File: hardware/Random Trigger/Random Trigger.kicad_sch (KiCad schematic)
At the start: 69 parts, among them J1 Eurorack Power, J10 Trigger Out B, J11 Inv Trigger Out B, J2 Noise In, J3 Noise Out, J4 Trigger In A, J5 Gate Out A, J6 Trigger Out A, J7 Inv Trigger Out A, J8 Trigger In B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

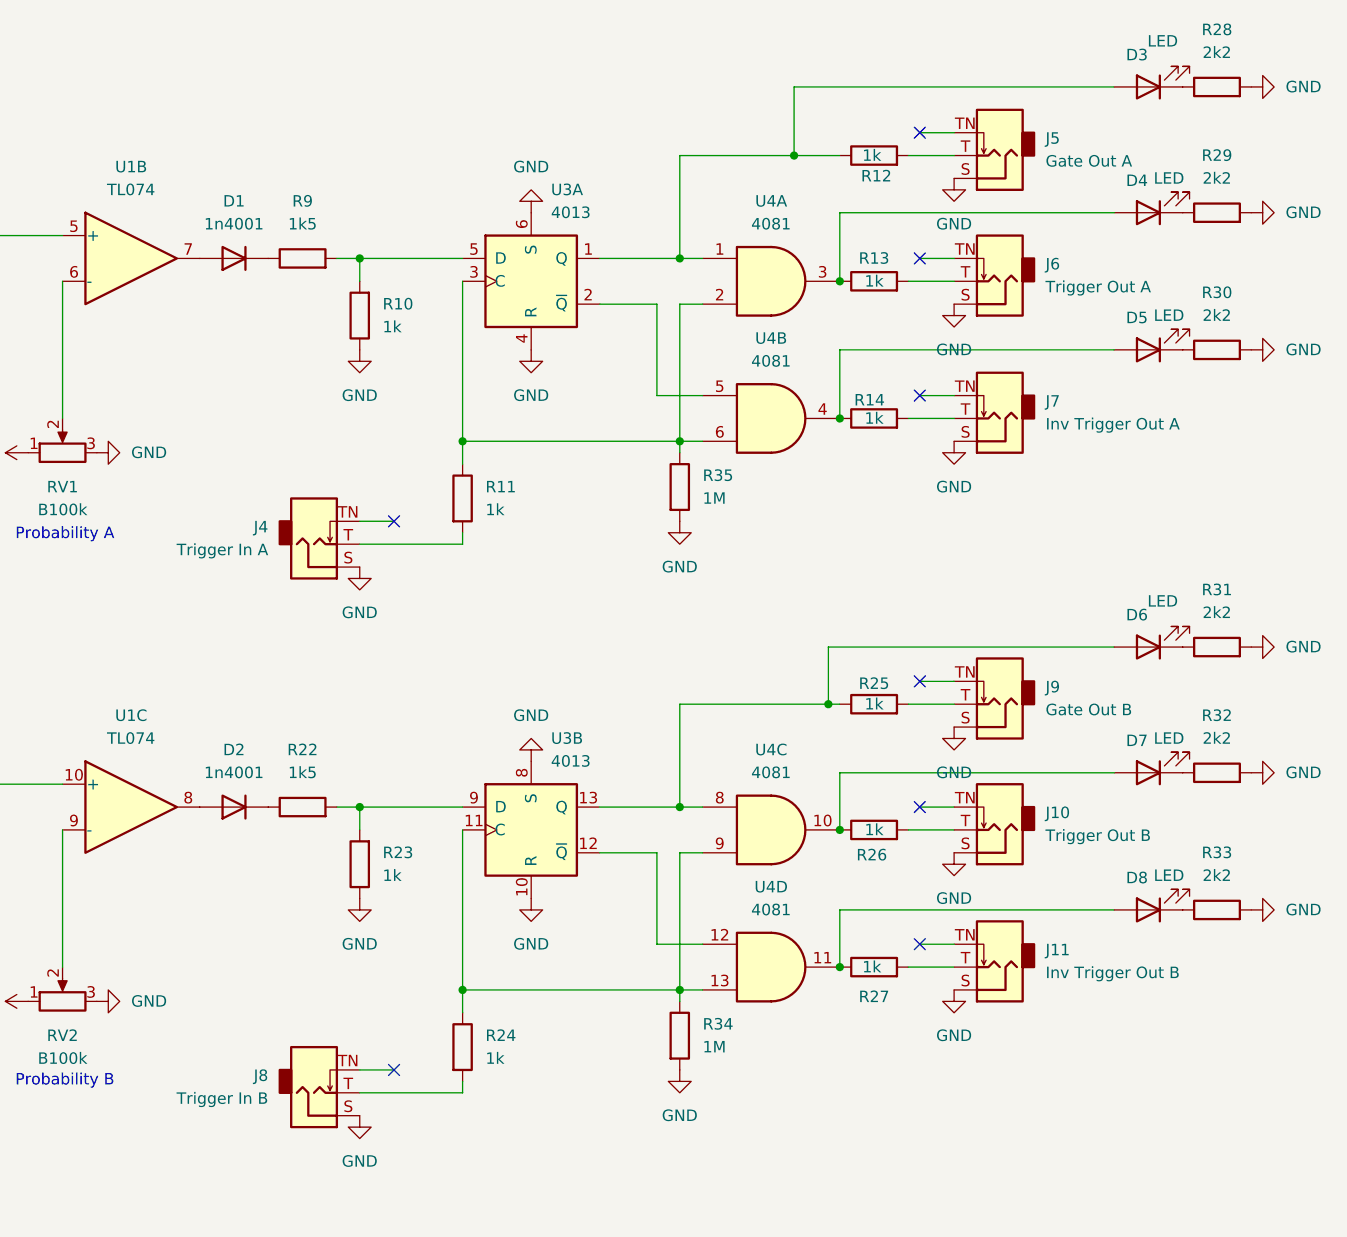
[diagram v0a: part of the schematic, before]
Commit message: Update schematic to match hardware
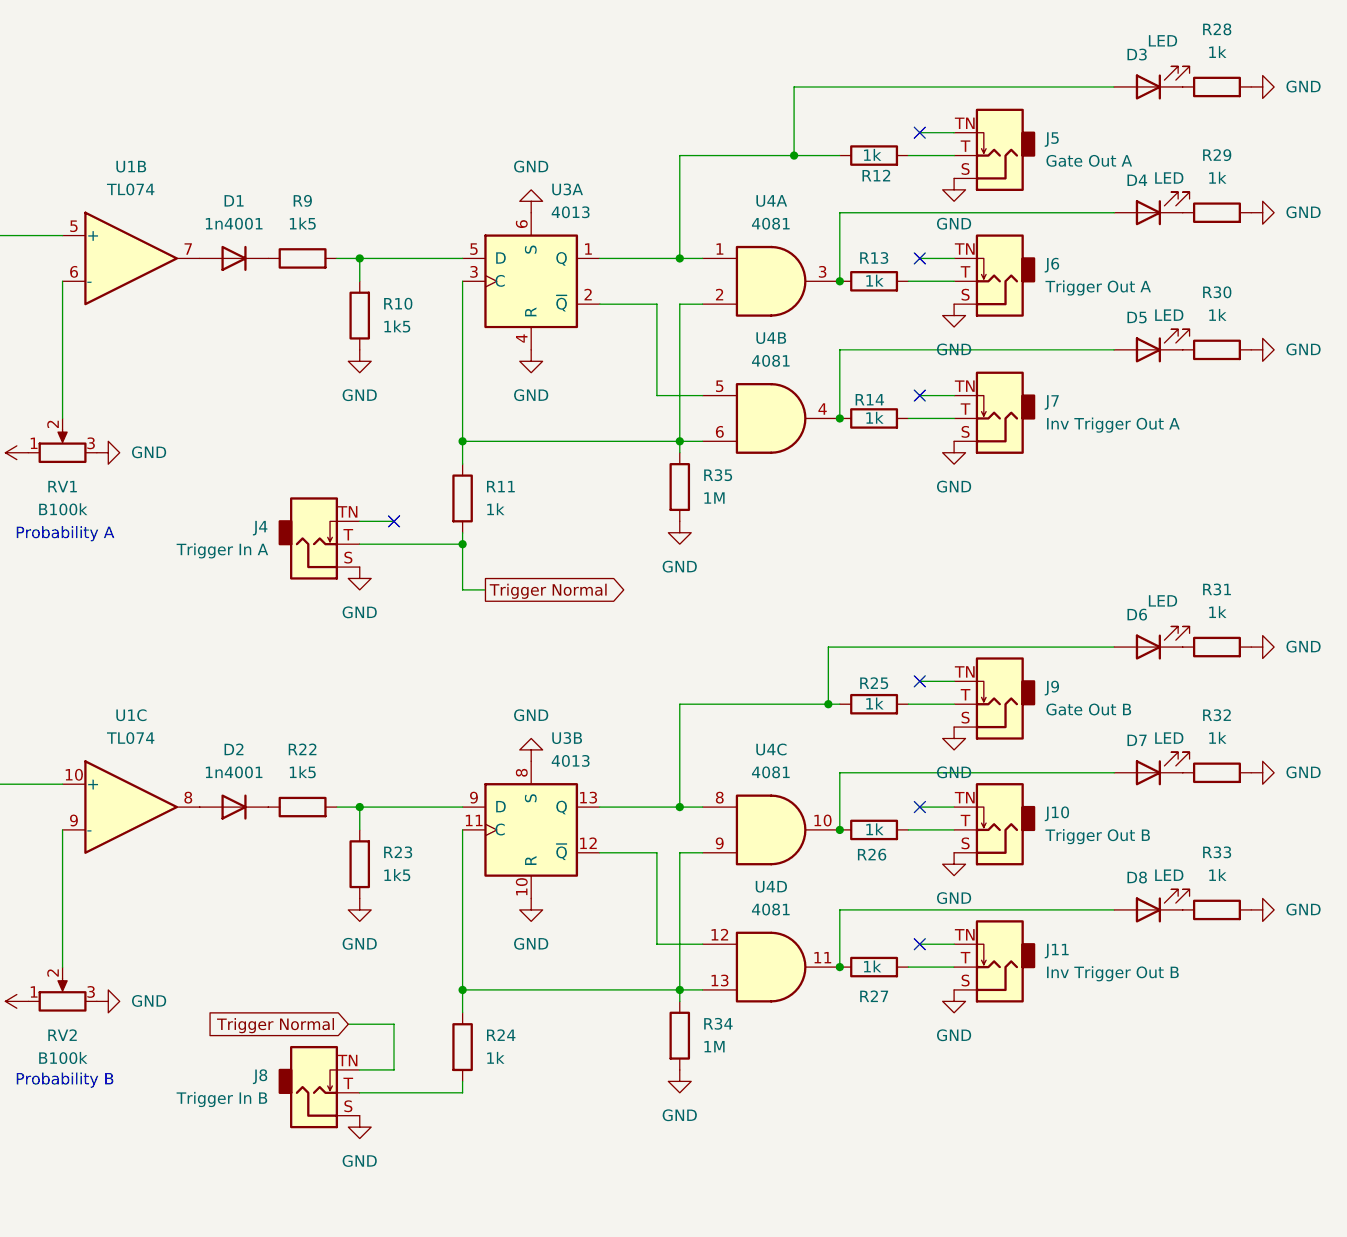
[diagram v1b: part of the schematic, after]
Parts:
- R10, R23: value 1k -> 1k5
- R28, R29, R30, R31, R32, R33: value 2k2 -> 1k
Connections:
- net Trigger Normal: now reaches J4.T, R11.2
- net Trigger Normal: now also J8.TN
- no-connect marks 11 -> 10
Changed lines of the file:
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@@
 	)
 	(junction
+		(at 180.34 68.58)
+		(diameter 0)
+		(color 0 0 0 0)
+	)
+	(junction
 		(at 119.38 36.83)
 		(diameter 0)
@@
 		(at 231.14 52.07)
 	)
-	(no_connect
-		(at 172.72 127)
-	)
 	(wire
 		(pts
@@
 	(wire
 		(pts
+			(xy 172.72 127) (xy 172.72 121.92)
+		)
+		(stroke
+			(width 0)
+			(type default)
+		)
+	)
+	(wire
+		(pts
 			(xy 85.09 162.56) (xy 100.33 162.56)
 		)
@@
 	(wire
 		(pts
+			(xy 172.72 121.92) (xy 167.64 121.92)
+		)
+		(stroke
+			(width 0)
+			(type default)
+		)
+	)
+	(wire
+		(pts
 			(xy 83.82 36.83) (xy 83.82 45.72)
 		)
@@
 	(wire
 		(pts
+			(xy 180.34 73.66) (xy 180.34 68.58)
+		)
+		(stroke
+			(width 0)
+			(type default)
+		)
+	)
+	(wire
+		(pts
 			(xy 252.73 46.99) (xy 222.25 46.99)
 		)
@@
 	(wire
 		(pts
+			(xy 182.88 73.66) (xy 180.34 73.66)
+		)
+		(stroke
+			(width 0)
+			(type default)
+		)
+	)
+	(wire
+		(pts
 			(xy 231.14 52.07) (xy 234.95 52.07)
 		)
@@
 		)
 	)
+	(global_label "Trigger Normal"
+		(shape input)
+		(at 167.64 121.92 180)
+		(fields_autoplaced yes)
+		(effects
+			(font
+				(size 1.27 1.27)
+			)
+			(justify right)
+		)
+		(property "Intersheetrefs" "${INTERSHEET_REFS}"
+			(at 150.3826 121.92 0)
+			(effects
+				(font
+					(size 1.27 1.27)
+				)
+				(justify right)
+				(hide yes)
+			)
+		)
+	)
+	(global_label "Trigger Normal"
+		(shape output)
+		(at 182.88 73.66 0)
+		(fields_autoplaced yes)
+		(effects
+			(font
+				(size 1.27 1.27)
+			)
+			(justify left)
+		)
+		(property "Intersheetrefs" "${INTERSHEET_REFS}"
+			(at 200.1374 73.66 0)
+			(effects
+				(font
+					(size 1.27 1.27)
+				)
+				(justify left)
+				(hide yes)
+			)
+		)
+	)
 	(symbol
 		(lib_id "power:GND")
@@
 			)
 		)
-		(property "Value" "1k"
+		(property "Value" "1k5"
 			(at 171.45 44.4499 0)
 			(effects
@@
 			)
 		)
-		(property "Value" "1k"
+		(property "Value" "1k5"
 			(at 171.45 105.4099 0)
 			(effects
@@
 			)
 		)
-		(property "Value" "2k2"
+		(property "Value" "1k"
 			(at 264.16 90.17 90)
 			(effects
@@
 			)
 		)
-		(property "Value" "2k2"
+		(property "Value" "1k"
 			(at 264.16 76.2 90)
 			(effects
@@
 			)
 		)
-		(property "Value" "2k2"
+		(property "Value" "1k"
 			(at 264.16 27.94 90)
 			(effects
@@
 			)
 		)
-		(property "Value" "2k2"
+		(property "Value" "1k"
 			(at 264.16 13.97 90)
 			(effects
@@
 			)
 		)
-		(property "Value" "2k2"
+		(property "Value" "1k"
 			(at 264.16 43.18 90)
 			(effects
@@
 			)
 		)
-		(property "Value" "2k2"
+		(property "Value" "1k"
 			(at 264.16 105.41 90)
 			(effects
